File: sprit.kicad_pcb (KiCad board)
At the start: 2 copper layers, 25.6 x 40 mm, 14 parts, among them J1 BARREL_JACK, J2 CONN_02X05, J3 CONN_01X03, Q1 2N7002, Q2 2N7002, U1 MC7808CDTRKG, U2 SN74LV1T126

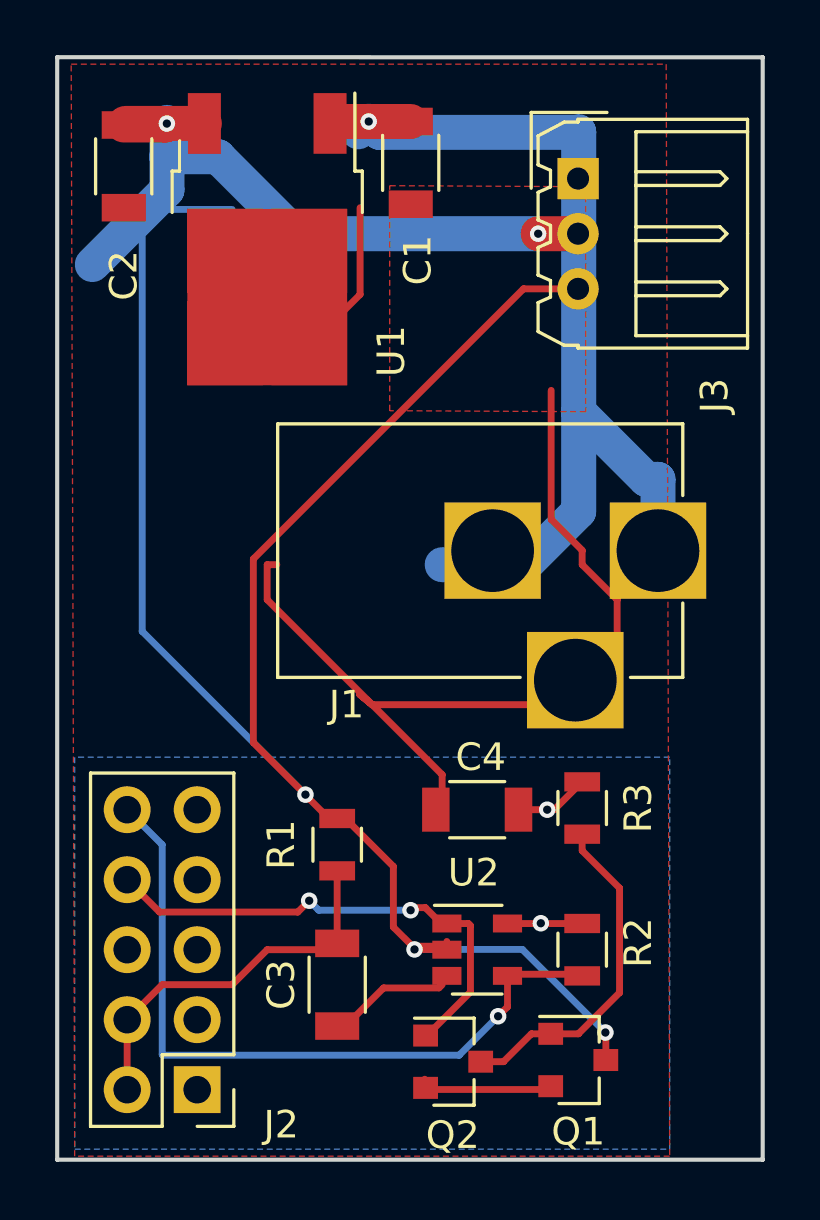
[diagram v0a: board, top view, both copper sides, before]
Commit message: finish layout rework started 4 years ago(!)
- recess barrel jack
- move J3 connector to opposite edge
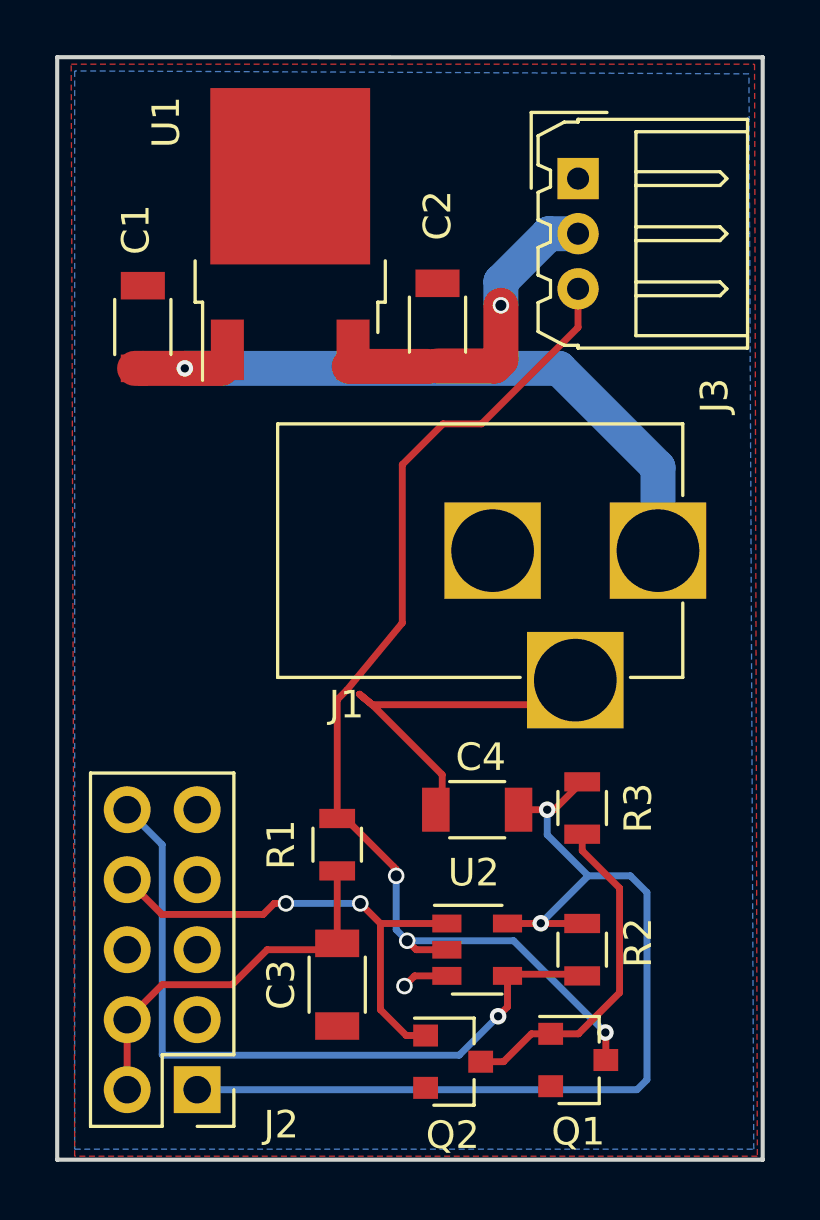
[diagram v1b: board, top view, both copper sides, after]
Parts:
- moved C2 12.8 mm to (166.2, 71.3), turned to 90 degrees
- moved C1 11.4 mm to (155.5, 71.4), turned to 90 degrees
- moved U1 0.85 mm to (160.9, 68.0), turned to 90 degrees
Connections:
- J2 pad 3: Net-(J2-Pad3) -> (no net)
- J2 pad 5: Net-(J2-Pad5) -> (no net)
- J2 pad 6: Net-(J2-Pad6) -> (no net)
- J2 pad 7: Net-(J2-Pad7) -> (no net)
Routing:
- net GND: track 54.1 -> 17.4 mm, vias 0 -> 1
- net +3V3: track 5.83 -> 36.9 mm
- net Net-(J3-Pad3): track 71.3 -> 40.7 mm
- net Net-(C2-Pad1): track 30.8 -> 11.7 mm, vias 2 -> 1
- net Net-(C1-Pad1): track 31.5 -> 24.9 mm
- added copper zone on B.Cu, net GND
- removed copper zone on B.Cu, net +3V3

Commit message: upgrade to kicad 6.0.7
- v0.2 as ordered from oshpark
- replace footprints
- add pdf of 2017 mouser order
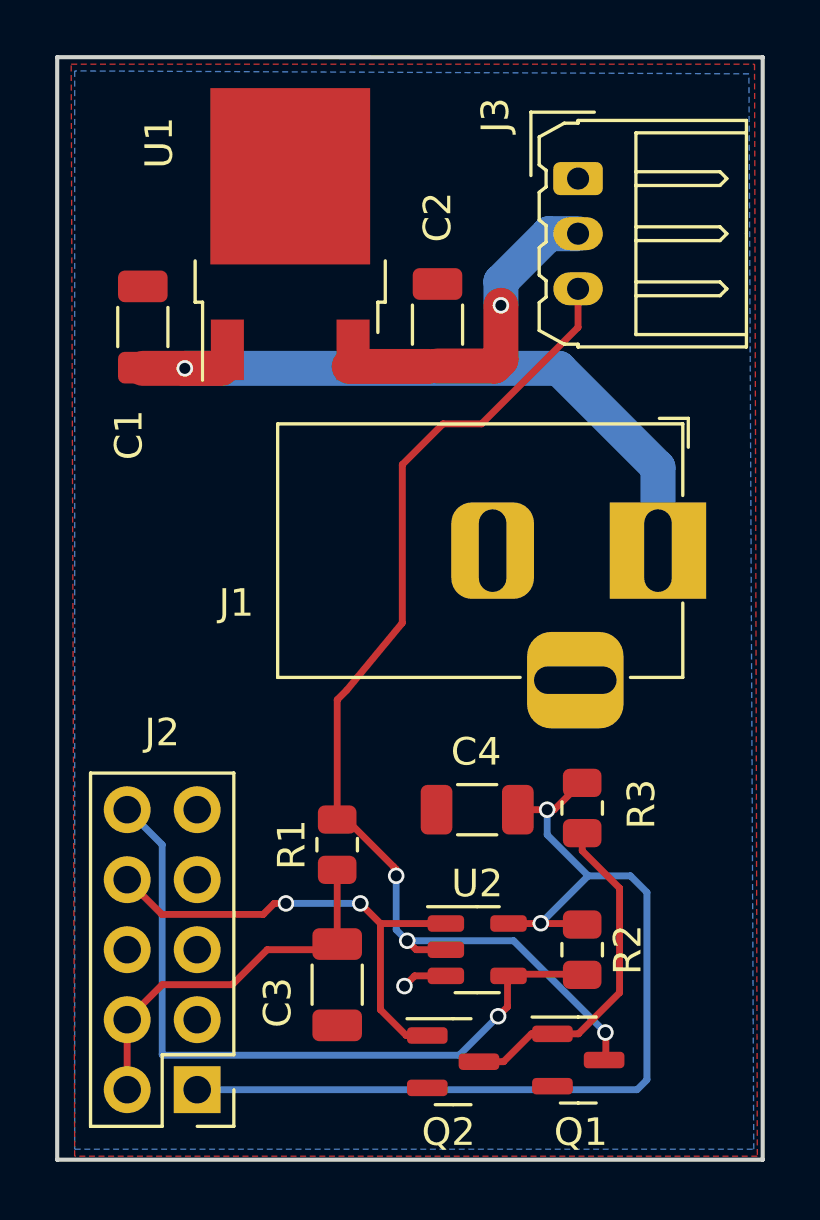
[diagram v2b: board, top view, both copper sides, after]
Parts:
- C1, C2, C3, C4: footprint Capacitors_SMD:C_1206 -> Capacitor_SMD:C_1206_3216Metric
- J1: footprint Connectors:BARREL_JACK -> Connector_BarrelJack:BarrelJack_Horizontal
- J2: footprint Pin_Headers:Pin_Header_Straight_2x05_Pitch2.54mm -> Connector_PinHeader_2.54mm:PinHeader_2x05_P2.54mm_Vertical
- J3: footprint Connectors_Molex:Molex_MicroLatch-53254-0370_03x2.00mm_Angled -> Connector_Molex:Molex_Micro-Latch_53254-0370_1x03_P2.00mm_Horizontal
- Q1, Q2: footprint TO_SOT_Packages_SMD:SOT-23 -> Package_TO_SOT_SMD:SOT-23
- R1, R2, R3: footprint Resistors_SMD:R_0805 -> Resistor_SMD:R_0805_2012Metric
- U1: footprint TO_SOT_Packages_SMD:TO-252-2 -> Package_TO_SOT_SMD:TO-252-2
- U2: footprint TO_SOT_Packages_SMD:SOT-23-5 -> Package_TO_SOT_SMD:SOT-23-5
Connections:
- J2 pad 3: (no net) -> unconnected-(J2-Pad3)
- J2 pad 5: (no net) -> unconnected-(J2-Pad5)
- J2 pad 6: (no net) -> unconnected-(J2-Pad6)
- J2 pad 7: (no net) -> unconnected-(J2-Pad7)
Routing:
- net GND: track 17.4 -> 1.69 mm
- net Net-(J2-Pad10): track 27.1 -> 26.4 mm
- net Net-(J3-Pad3): track 40.7 -> 40.1 mm
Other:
- net class Default removed
- net class power removed
- board text added: "sprit v0.2 cdint.com"
